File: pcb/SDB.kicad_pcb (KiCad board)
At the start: 2 copper layers, 77.5 x 50.8 mm, 64 parts, among them J1 Conn_01x02_Pin, J10 Conn_01x03_Pin, J11 Conn_01x04_Socket, J12 Conn_01x03_Pin, J13 Conn_01x02_Pin, J14 Conn_01x02_Pin, J15 Conn_01x02_Pin, J16 Conn_01x02_Pin, J17 Conn_01x04_Socket, J18 Conn_01x03_Pin, J19 Conn_01x03_Pin, J2 Conn_01x10_Socket, J20 Conn_01x03_Pin, J21 Conn_01x02_Pin, J22 Conn_01x03_Pin, J23 Conn_01x02_Pin, J24 Conn_01x02_Socket, J25 Conn_01x03_Socket, J3 Conn_01x10_Socket, J4 Conn_02x02_Counter_Clockwise, J5 Conn_02x02_Counter_Clockwise, J6 Conn_02x02_Counter_Clockwise, J7 Conn_02x02_Counter_Clockwise, J8 Conn_02x02_Counter_Clockwise, J9 Conn_02x02_Counter_Clockwise, SW1 SW_SPST, SW2 SW_SPST, SW3 SW_SPST, SW4 SW_SPST, SW5 SW_Coded_SH-7050, SW6 SW_DIP_x02

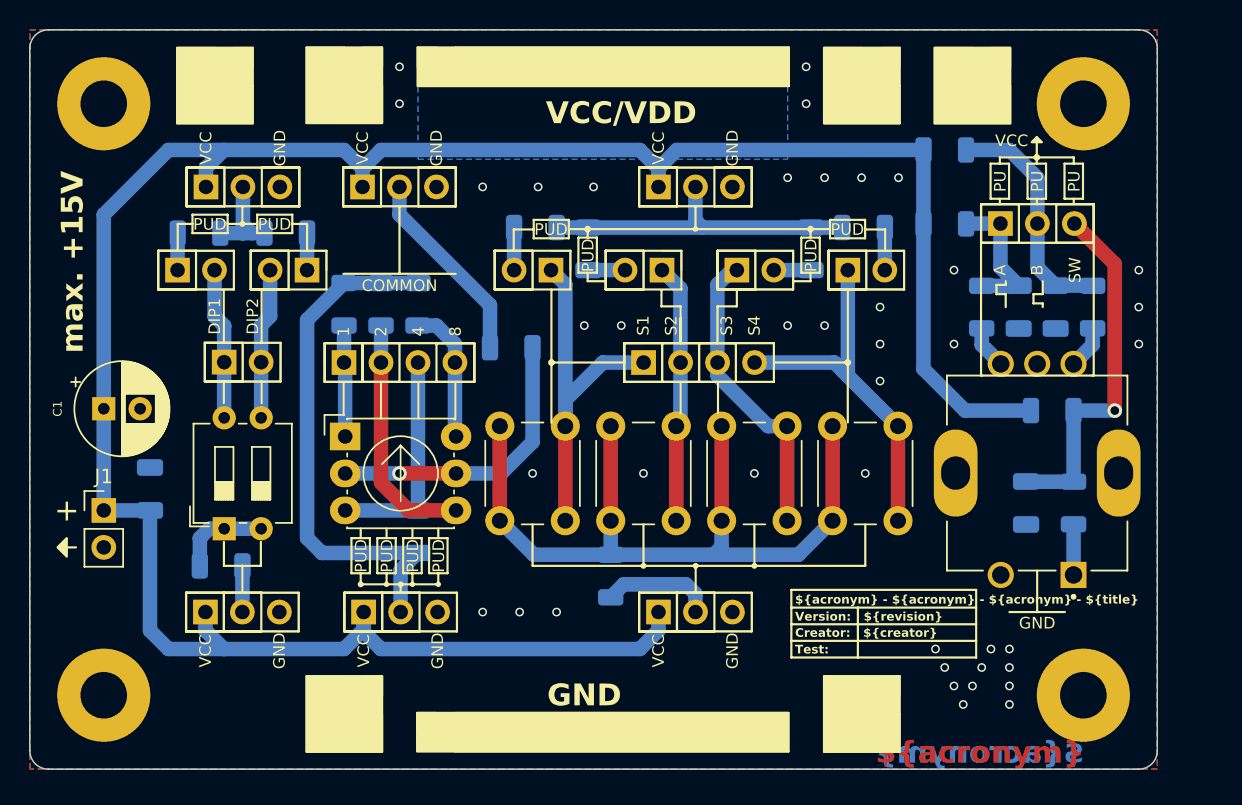
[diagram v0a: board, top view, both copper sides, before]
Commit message: Add reverse polarity protection
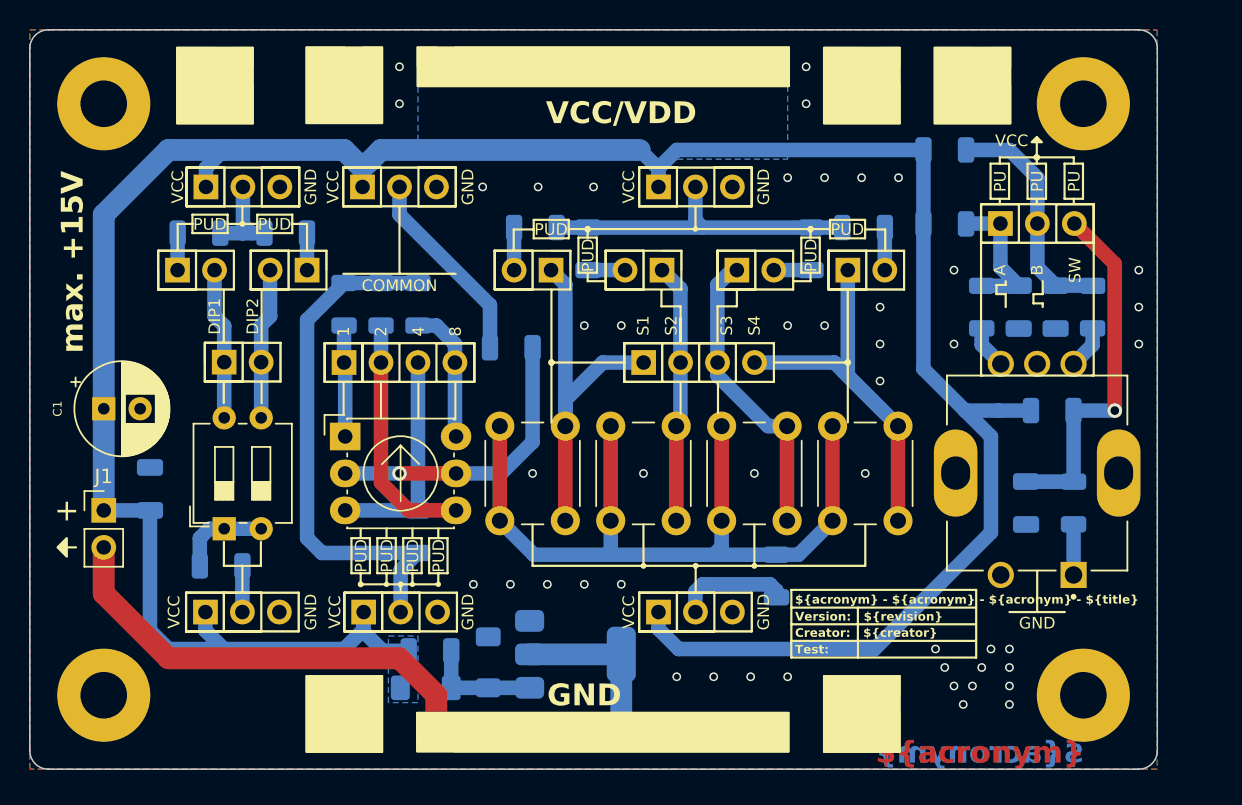
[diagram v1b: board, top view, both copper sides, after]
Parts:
- added D1: BAT43, Diode_SMD:D_MiniMELF, B.Cu at (146.6, 121.4)
- added D2: BZ5V1, Diode_SMD:D_MiniMELF, B.Cu at (150.9, 119.7)
- added Q1: BUK7880-55A, Package_TO_SOT_SMD:SOT-223-3_TabPin2, B.Cu at (156.9, 119.1)
- added R19: 1k, Resistor_SMD:R_1206_3216Metric, B.Cu at (146.9, 118.9)
- FID4: footprint Images:QR_0x007e -> Images:QR_0x007e_very_small
- moved R1 11.4 mm to (170.7, 113.7)
- moved FID4 2.34 mm to (175.9, 114.3)
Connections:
- J1 pad 2: GND -> Net-(J1-Pin_2)
- J3 pad 1: GND -> Net-(J1-Pin_2)
- J3 pad 10: GND -> Net-(J1-Pin_2)
- J3 pad 2: GND -> Net-(J1-Pin_2)
- J3 pad 3: GND -> Net-(J1-Pin_2)
- J3 pad 4: GND -> Net-(J1-Pin_2)
- J3 pad 5: GND -> Net-(J1-Pin_2)
- J3 pad 6: GND -> Net-(J1-Pin_2)
- J3 pad 7: GND -> Net-(J1-Pin_2)
- J3 pad 8: GND -> Net-(J1-Pin_2)
- J3 pad 9: GND -> Net-(J1-Pin_2)
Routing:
- net Net-(J1-Pin_2): track 0.00 -> 43.1 mm
- net VCC: track 166.4 -> 184.5 mm
- net Net-(D1-A): track 0.00 -> 7.92 mm
- net GND: vias 41 -> 47
- added copper zone on B.Cu, net Net-(J1-Pin_2)
